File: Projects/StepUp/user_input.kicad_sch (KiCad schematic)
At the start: 3 parts, among them J11 Conn_02x03_Counter_Clockwise

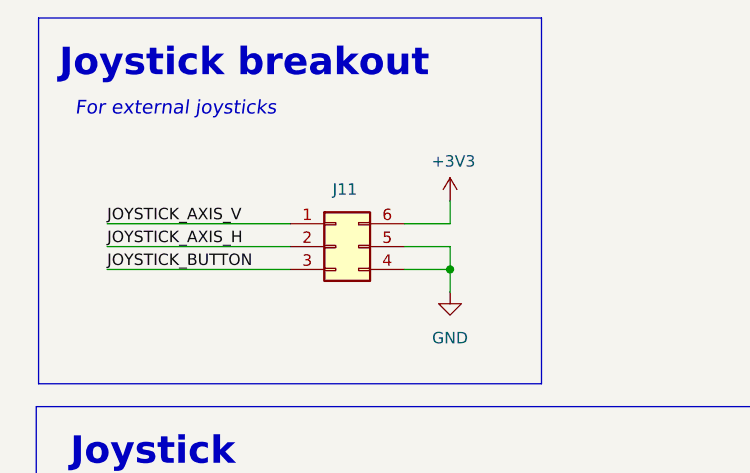
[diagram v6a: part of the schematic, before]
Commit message: feat(layout): Blocks organised
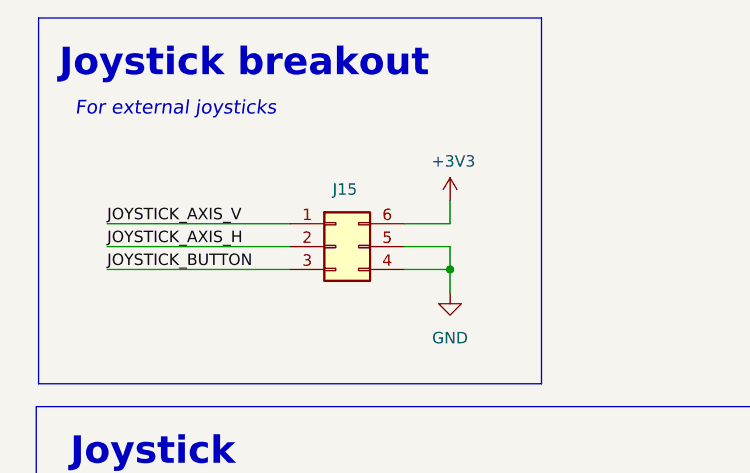
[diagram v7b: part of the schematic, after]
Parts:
- renumbered J11 to J15
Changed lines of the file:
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@@
 		(dnp no)
 		(fields_autoplaced yes)
-		(property "Reference" "#PWR094"
+		(property "Reference" "#PWR096"
 			(at 109.22 80.01 0)
 			(effects
@@
 			(project "StepUp"
 				(path "/e0cca1c7-c263-49eb-8c40-74000ebe5285/62dd6998-8b69-42c0-9c2f-b18953d44bc4"
-					(reference "#PWR094")
+					(reference "#PWR096")
 					(unit 1)
 				)
@@
 		(dnp no)
 		(fields_autoplaced yes)
-		(property "Reference" "#PWR098"
+		(property "Reference" "#PWR0100"
 			(at 167.64 140.97 0)
 			(effects
@@
 			(project "StepUp"
 				(path "/e0cca1c7-c263-49eb-8c40-74000ebe5285/62dd6998-8b69-42c0-9c2f-b18953d44bc4"
-					(reference "#PWR098")
+					(reference "#PWR0100")
 					(unit 1)
 				)
@@
 		(dnp no)
 		(fields_autoplaced yes)
-		(property "Reference" "#PWR097"
+		(property "Reference" "#PWR099"
 			(at 149.86 104.14 0)
 			(effects
@@
 			(project "StepUp"
 				(path "/e0cca1c7-c263-49eb-8c40-74000ebe5285/62dd6998-8b69-42c0-9c2f-b18953d44bc4"
-					(reference "#PWR097")
+					(reference "#PWR099")
 					(unit 1)
 				)
@@
 		(dnp no)
 		(fields_autoplaced yes)
-		(property "Reference" "#PWR095"
+		(property "Reference" "#PWR097"
 			(at 125.73 140.97 0)
 			(effects
@@
 			(project "StepUp"
 				(path "/e0cca1c7-c263-49eb-8c40-74000ebe5285/62dd6998-8b69-42c0-9c2f-b18953d44bc4"
-					(reference "#PWR095")
+					(reference "#PWR097")
 					(unit 1)
 				)
@@
 		(on_board yes)
 		(dnp no)
-		(property "Reference" "J11"
+		(property "Reference" "J15"
 			(at 97.536 62.23 0)
 			(effects
@@
 			(project "StepUp"
 				(path "/e0cca1c7-c263-49eb-8c40-74000ebe5285/62dd6998-8b69-42c0-9c2f-b18953d44bc4"
-					(reference "J11")
+					(reference "J15")
 					(unit 1)
 				)
@@
 		(on_board yes)
 		(dnp no)
-		(property "Reference" "#PWR093"
+		(property "Reference" "#PWR095"
 			(at 109.22 67.31 0)
 			(effects
@@
 			(project "StepUp"
 				(path "/e0cca1c7-c263-49eb-8c40-74000ebe5285/62dd6998-8b69-42c0-9c2f-b18953d44bc4"
-					(reference "#PWR093")
+					(reference "#PWR095")
 					(unit 1)
 				)
@@
 		(on_board yes)
 		(dnp no)
-		(property "Reference" "#PWR096"
+		(property "Reference" "#PWR098"
 			(at 128.27 105.41 0)
 			(effects
@@
 			(project "StepUp"
 				(path "/e0cca1c7-c263-49eb-8c40-74000ebe5285/62dd6998-8b69-42c0-9c2f-b18953d44bc4"
-					(reference "#PWR096")
-					(unit 1)
-				)
+					(reference "#PWR098")
+					(unit 1)
+				)

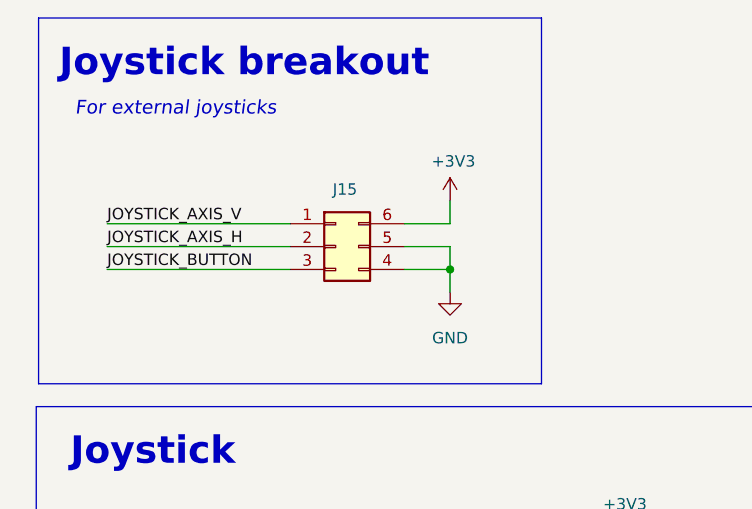
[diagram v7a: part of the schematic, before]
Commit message: feat(tidy): Bigger PMOS, added footprints
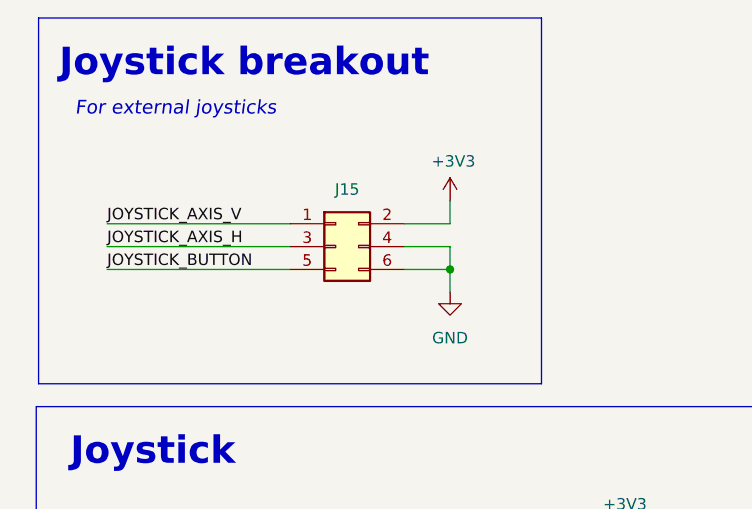
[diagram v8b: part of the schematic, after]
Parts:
- removed J15: Conn_02x03_Counter_Clockwise, Connector_PinHeader_2.54mm:PinHeader_2x03_P2.54mm_Vertical, symbol Connector_Generic:Conn_02x03_Counter_Clockwise
- added J15: Conn_02x03_Odd_Even, Connector_PinHeader_2.54mm:PinHeader_2x03_P2.54mm_Vertical, symbol Connector_Generic:Conn_02x03_Odd_Even
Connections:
- net +3V3: now also J15.2 (Pin_2)
- net GND: now also J15.4 (Pin_4), J15.6 (Pin_6)
- net JOYSTSICK_AXIS_H: now also J15.3 (Pin_3)
- net JOYSTSICK_AXIS_V: now also J15.1 (Pin_1)
- net JOYSTSICK_BUTTON: now also J15.5 (Pin_5)
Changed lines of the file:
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@@
 				(size 1.524 1.524)
 				(italic yes)
-				(color 29 232 255 1)
+				(color 132 132 132 1)
 			)
 		)
@@
 				(justify right)
 				(hide yes)
+			)
+		)
+	)
+	(symbol
+		(lib_id "Connector_Generic:Conn_02x03_Odd_Even")
+		(at 96.52 68.58 0)
+		(unit 1)
+		(exclude_from_sim no)
+		(in_bom yes)
+		(on_board yes)
+		(dnp no)
+		(fields_autoplaced yes)
+		(property "Reference" "J15"
+			(at 97.79 62.23 0)
+			(effects
+				(font
+					(size 1.27 1.27)
+				)
+			)
+		)
+		(property "Value" "Conn_02x03_Odd_Even"
+			(at 97.79 62.23 0)
+			(effects
+				(font
+					(size 1.27 1.27)
+				)
+				(hide yes)
+			)
+		)
+		(property "Footprint" "Connector_PinHeader_2.54mm:PinHeader_2x03_P2.54mm_Vertical"
+			(at 96.52 68.58 0)
+			(effects
+				(font
+					(size 1.27 1.27)
+				)
+				(hide yes)
+			)
+		)
+		(property "Datasheet" "~"
+			(at 96.52 68.58 0)
+			(effects
+				(font
+					(size 1.27 1.27)
+				)
+				(hide yes)
+			)
+		)
+		(property "Description" "Generic connector, double row, 02x03, odd/even pin numbering scheme (row 1 odd numbers, row 2 even numbers), script generated (kicad-library-utils/schlib/autogen/connector/)"
+			(at 96.52 68.58 0)
+			(effects
+				(font
+					(size 1.27 1.27)
+				)
+				(hide yes)
+			)
+		)
+		(pin "4"
+		)
+		(pin "3"
+		)
+		(pin "2"
+		)
+		(pin "1"
+		)
+		(pin "5"
+		)
+		(pin "6"
+		)
+		(instances
+			(project "StepUp"
+				(path "/e0cca1c7-c263-49eb-8c40-74000ebe5285/62dd6998-8b69-42c0-9c2f-b18953d44bc4"
+					(reference "J15")
+					(unit 1)
+				)
 			)
 		)
@@
 		(dnp no)
 		(fields_autoplaced yes)
-		(property "Reference" "#PWR096"
+		(property "Reference" "#PWR0101"
 			(at 109.22 80.01 0)
 			(effects
@@
 			(project "StepUp"
 				(path "/e0cca1c7-c263-49eb-8c40-74000ebe5285/62dd6998-8b69-42c0-9c2f-b18953d44bc4"
-					(reference "#PWR096")
+					(reference "#PWR0101")
 					(unit 1)
 				)
@@
 		(dnp no)
 		(fields_autoplaced yes)
-		(property "Reference" "#PWR0100"
+		(property "Reference" "#PWR0105"
 			(at 167.64 140.97 0)
 			(effects
@@
 			(project "StepUp"
 				(path "/e0cca1c7-c263-49eb-8c40-74000ebe5285/62dd6998-8b69-42c0-9c2f-b18953d44bc4"
-					(reference "#PWR0100")
+					(reference "#PWR0105")
 					(unit 1)
 				)
@@
 		(dnp no)
 		(fields_autoplaced yes)
-		(property "Reference" "#PWR099"
+		(property "Reference" "#PWR0104"
 			(at 149.86 104.14 0)
 			(effects
@@
 			(project "StepUp"
 				(path "/e0cca1c7-c263-49eb-8c40-74000ebe5285/62dd6998-8b69-42c0-9c2f-b18953d44bc4"
-					(reference "#PWR099")
+					(reference "#PWR0104")
 					(unit 1)
 				)
@@
 		(dnp no)
 		(fields_autoplaced yes)
-		(property "Reference" "#PWR097"
+		(property "Reference" "#PWR0102"
 			(at 125.73 140.97 0)
 			(effects
@@
 			(project "StepUp"
 				(path "/e0cca1c7-c263-49eb-8c40-74000ebe5285/62dd6998-8b69-42c0-9c2f-b18953d44bc4"
-					(reference "#PWR097")
-					(unit 1)
-				)
-			)
-		)
-	)
-	(symbol
-		(lib_id "Connector_Generic:Conn_02x03_Counter_Clockwise")
-		(at 96.52 68.58 0)
-		(unit 1)
-		(exclude_from_sim no)
-		(in_bom yes)
-		(on_board yes)
-		(dnp no)
-		(property "Reference" "J15"
-			(at 97.536 62.23 0)
-			(effects
-				(font
-					(size 1.27 1.27)
-				)
-			)
-		)
-		(property "Value" "Conn_02x03_Counter_Clockwise"
-			(at 98.044 75.184 0)
-			(effects
-				(font
-					(size 1.27 1.27)
-				)
-				(hide yes)
-			)
-		)
-		(property "Footprint" "Connector_PinHeader_2.54mm:PinHeader_2x03_P2.54mm_Vertical"
-			(at 96.52 68.58 0)
-			(effects
-				(font
-					(size 1.27 1.27)
-				)
-				(hide yes)
-			)
-		)
-		(property "Datasheet" "~"
-			(at 96.52 68.58 0)
-			(effects
-				(font
-					(size 1.27 1.27)
-				)
-				(hide yes)
-			)
-		)
-		(property "Description" "Generic connector, double row, 02x03, counter clockwise pin numbering scheme (similar to DIP package numbering), script generated (kicad-library-utils/schlib/autogen/connector/)"
-			(at 96.52 68.58 0)
-			(effects
-				(font
-					(size 1.27 1.27)
-				)
-				(hide yes)
-			)
-		)
-		(pin "5"
-		)
-		(pin "2"
-		)
-		(pin "6"
-		)
-		(pin "1"
-		)
-		(pin "4"
-		)
-		(pin "3"
-		)
-		(instances
-			(project "StepUp"
-				(path "/e0cca1c7-c263-49eb-8c40-74000ebe5285/62dd6998-8b69-42c0-9c2f-b18953d44bc4"
-					(reference "J15")
+					(reference "#PWR0102")
 					(unit 1)
 				)
@@
 		(on_board yes)
 		(dnp no)
-		(property "Reference" "#PWR095"
+		(property "Reference" "#PWR0100"
 			(at 109.22 67.31 0)
 			(effects
@@
 			(project "StepUp"
 				(path "/e0cca1c7-c263-49eb-8c40-74000ebe5285/62dd6998-8b69-42c0-9c2f-b18953d44bc4"
-					(reference "#PWR095")
+					(reference "#PWR0100")
 					(unit 1)
 				)
@@
 		(on_board yes)
 		(dnp no)
-		(property "Reference" "#PWR098"
+		(property "Reference" "#PWR0103"
 			(at 128.27 105.41 0)
 			(effects
@@
 			(project "StepUp"
 				(path "/e0cca1c7-c263-49eb-8c40-74000ebe5285/62dd6998-8b69-42c0-9c2f-b18953d44bc4"
-					(reference "#PWR098")
+					(reference "#PWR0103")
 					(unit 1)
 				)
